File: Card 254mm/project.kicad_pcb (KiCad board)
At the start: 2 copper layers, 51.5 x 22 mm, 9 parts, among them J1 Conn_01x04, J2 Conn_01x10, J3 Conn_01x10, J4 Conn_01x10, J5 Conn_01x10, J6 Conn_01x10, U1 24LC32, X0 Card Edge

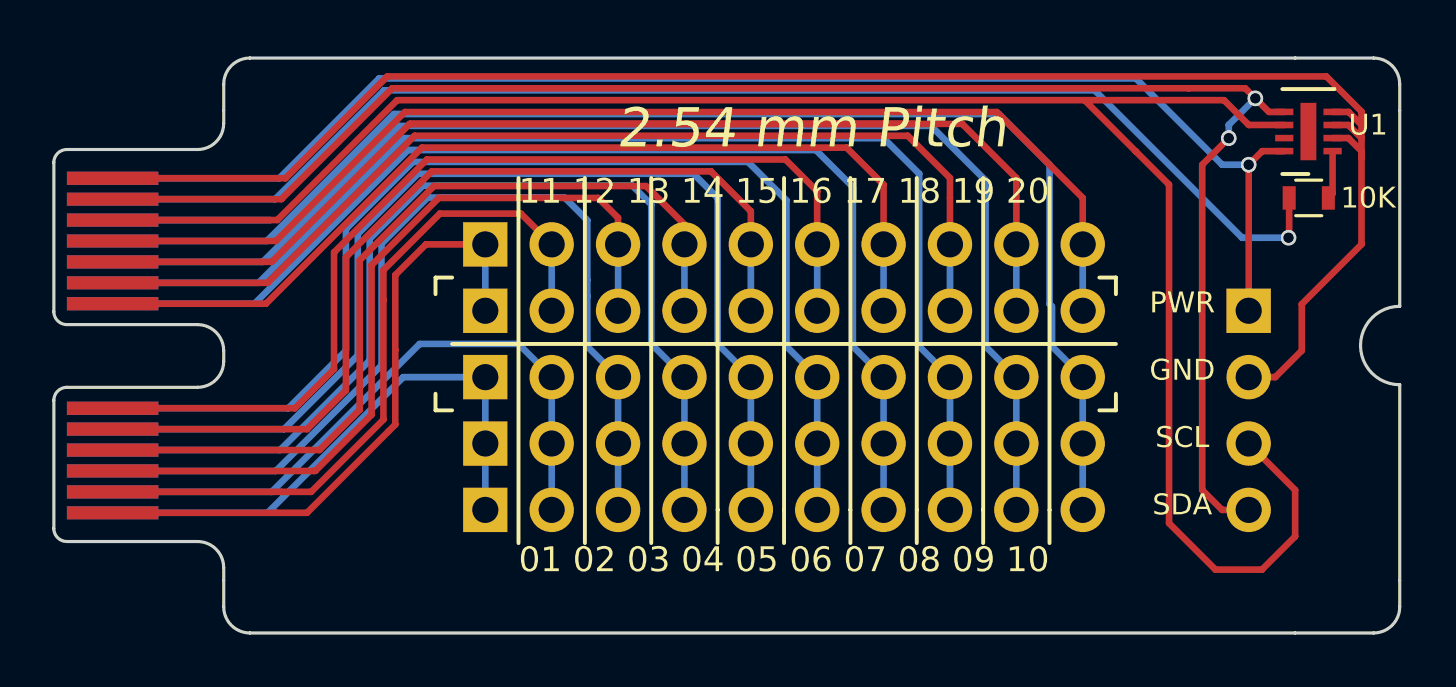
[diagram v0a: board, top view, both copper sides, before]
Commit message: EEPROM footprint update
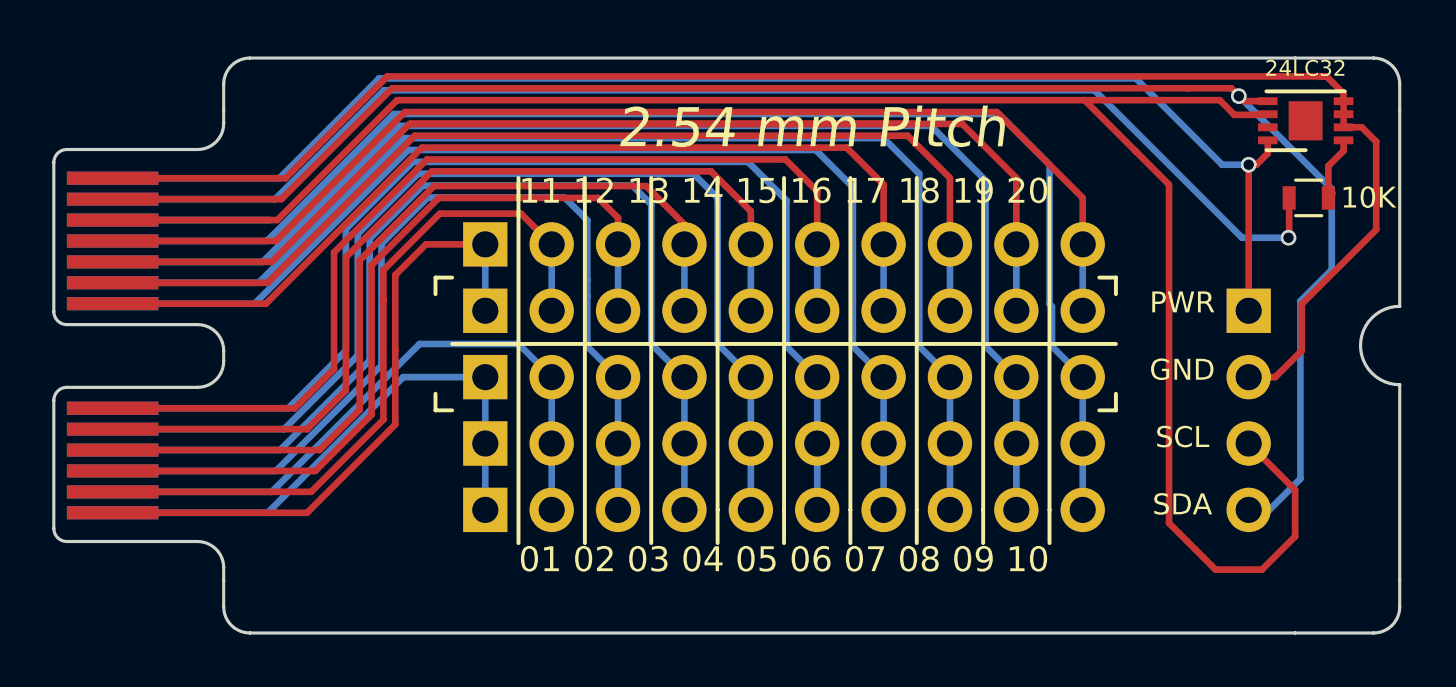
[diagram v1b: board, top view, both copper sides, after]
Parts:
- U1: footprint Package_DFN_QFN:DFN-8-1EP_2x3mm_P0.5mm_EP0.61x2.2mm -> footprints:DFN-8-1EP_3x2mm
- moved U1 0.43 mm to (47.9, -18.7)
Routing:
- net GND: track 66.7 -> 63.6 mm
- net Net-(R1-Pad1): track 1.86 -> 2.67 mm
- net /D3_SCL: track 75.0 -> 74.2 mm
- net /D2_SDA: track 64.9 -> 65.3 mm, vias 2 -> 1

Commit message: updates
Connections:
- J1 pad 1: +5V -> GND
- J1 pad 2: GND -> +5V
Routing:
- net +5V: track 53.4 -> 58.5 mm
- net GND: track 63.6 -> 61.7 mm
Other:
- board text added: "2.54mm Pitch"
- board text added: "GND PWR SCL SDA"
- board text removed: "2.54 mm Pitch"
- board text removed: "PWR GND SCL SDA"
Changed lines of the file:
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@@
     (thickness 1.6)
     (drawings 50)
-    (tracks 236)
+    (tracks 239)
     (zones 0)
     (modules 9)
@@
     )
     (pad 1 thru_hole rect (at 0 0) (size 1.7 1.7) (drill 1) (layers *.Cu *.Mask)
+      (net 22 GND))
+    (pad 2 thru_hole oval (at 0 2.54) (size 1.7 1.7) (drill 1) (layers *.Cu *.Mask)
       (net 24 +5V))
-    (pad 2 thru_hole oval (at 0 2.54) (size 1.7 1.7) (drill 1) (layers *.Cu *.Mask)
-      (net 22 GND))
     (pad 3 thru_hole oval (at 0 5.08) (size 1.7 1.7) (drill 1) (layers *.Cu *.Mask)
       (net 23 /D3_SCL))
@@
     )
   )
-  (gr_text "PWR\n\nGND\n\nSCL\n\nSDA" (at 43.18 -7.874) (layer B.SilkS)
+  (gr_text "GND\n\nPWR\n\nSCL\n\nSDA" (at 43.18 -7.874) (layer B.SilkS)
     (effects (font (size 0.8 0.8) (thickness 0.15)) (justify mirror))
   )
-  (gr_text "PWR\n\nGND\n\nSCL\n\nSDA" (at 43.18 -7.874) (layer F.SilkS)
+  (gr_text "GND\n\nPWR\n\nSCL\n\nSDA" (at 43.18 -7.874) (layer F.SilkS)
     (effects (font (size 0.8 0.8) (thickness 0.15)))
   )
@@
   )
   (gr_line (start 9.75 -19.5) (end 9.75 -0.5) (layer Dwgs.User) (width 0.1))
-  (gr_text "2.54 mm Pitch" (at 29 -18.415) (layer F.SilkS)
+  (gr_text "2.54mm Pitch" (at 29 -18.415) (layer F.SilkS)
     (effects (font (size 1.5 1.5) (thickness 0.25) italic))
   )
@@
   (segment (start 8.707934 -15.7) (end 12.950003 -19.94207) (width 0.254) (layer F.Cu) (net 21))
   (segment (start 2.25 -15.7) (end 8.707934 -15.7) (width 0.254) (layer F.Cu) (net 21) (status 10))
-  (segment (start 46.45 -19.45) (end 45.55 -19.45) (width 0.254) (layer F.Cu) (net 21))
+  (segment (start 46.45 -19.45) (end 45.55 -19.45) (width 0.254) (layer F.Cu) (net 21) (status 10))
   (segment (start 45.05793 -19.94207) (end 43.423864 -19.94207) (width 0.254) (layer F.Cu) (net 21))
   (via (at 45.343356 -19.643356) (size 0.6) (drill 0.4) (layers F.Cu B.Cu) (net 21))
@@
   (segment (start 48.9 -13) (end 47.7 -11.8) (width 0.254) (layer B.Cu) (net 21))
   (segment (start 47.7 -11.8) (end 47.7 -5) (width 0.254) (layer B.Cu) (net 21))
-  (segment (start 46.51 -3.81) (end 45.72 -3.81) (width 0.254) (layer B.Cu) (net 21))
-  (segment (start 47.7 -5) (end 46.51 -3.81) (width 0.254) (layer B.Cu) (net 21))
+  (segment (start 46.51 -3.81) (end 45.72 -3.81) (width 0.254) (layer B.Cu) (net 21) (status 30))
+  (segment (start 47.7 -5) (end 46.51 -3.81) (width 0.254) (layer B.Cu) (net 21) (status 20))
   (segment (start 8.865867 -16.5) (end 12.761946 -20.39608) (width 0.254) (layer F.Cu) (net 22))
   (segment (start 2.25 -16.5) (end 8.865867 -16.5) (width 0.254) (layer F.Cu) (net 22) (status 10))
-  (segment (start 49.35 -19.45) (end 49.35 -19.75) (width 0.254) (layer F.Cu) (net 22))
+  (segment (start 49.35 -19.45) (end 49.35 -19.75) (width 0.254) (layer F.Cu) (net 22) (status 10))
   (segment (start 48.70392 -20.39608) (end 48.49608 -20.39608) (width 0.254) (layer F.Cu) (net 22))
   (segment (start 49.35 -19.75) (end 48.70392 -20.39608) (width 0.254) (layer F.Cu) (net 22))
   (segment (start 48.49608 -20.39608) (end 48.69192 -20.39608) (width 0.254) (layer F.Cu) (net 22))
   (segment (start 12.761946 -20.39608) (end 48.49608 -20.39608) (width 0.254) (layer F.Cu) (net 22))
-  (segment (start 49.35 -19.45) (end 49.35 -18.95) (width 0.254) (layer F.Cu) (net 22))
-  (segment (start 49.35 -18.95) (end 49.35 -18.45) (width 0.254) (layer F.Cu) (net 22))
-  (segment (start 46.736 -8.89) (end 45.72 -8.89) (width 0.254) (layer F.Cu) (net 22))
-  (segment (start 47.752 -9.906) (end 46.736 -8.89) (width 0.254) (layer F.Cu) (net 22))
-  (segment (start 50.6 -14.532) (end 47.752 -11.684) (width 0.254) (layer F.Cu) (net 22))
-  (segment (start 47.752 -11.684) (end 47.752 -9.906) (width 0.254) (layer F.Cu) (net 22))
+  (segment (start 49.35 -19.45) (end 49.35 -18.95) (width 0.254) (layer F.Cu) (net 22) (status 30))
+  (segment (start 49.35 -18.95) (end 49.35 -18.45) (width 0.254) (layer F.Cu) (net 22) (status 30))
   (segment (start 50.6 -17.9) (end 50.6 -14.532) (width 0.254) (layer F.Cu) (net 22))
   (segment (start 50.05 -18.45) (end 50.6 -17.9) (width 0.254) (layer F.Cu) (net 22))
-  (segment (start 49.35 -18.45) (end 50.05 -18.45) (width 0.254) (layer F.Cu) (net 22))
+  (segment (start 49.35 -18.45) (end 50.05 -18.45) (width 0.254) (layer F.Cu) (net 22) (status 10))
+  (segment (start 47.498 -11.43) (end 47.884 -11.816) (width 0.254) (layer F.Cu) (net 22))
+  (segment (start 45.72 -11.43) (end 47.498 -11.43) (width 0.254) (layer F.Cu) (net 22))
+  (segment (start 47.884 -11.816) (end 47.752 -11.684) (width 0.254) (layer F.Cu) (net 22))
+  (segment (start 50.6 -14.532) (end 47.884 -11.816) (width 0.254) (layer F.Cu) (net 22))
   (segment (start 13.13806 -19.48806) (end 39.43994 -19.48806) (width 0.254) (layer F.Cu) (net 23))
   (segment (start 8.55 -14.9) (end 13.13806 -19.48806) (width 0.254) (layer F.Cu) (net 23))
@@
   (segment (start 45.72 -6.35) (end 47.498 -4.572) (width 0.254) (layer F.Cu) (net 23) (status 10))
   (segment (start 45.172999 -18.927001) (end 44.61194 -19.48806) (width 0.254) (layer F.Cu) (net 23))
-  (segment (start 46.327001 -18.927001) (end 45.172999 -18.927001) (width 0.254) (layer F.Cu) (net 23))
-  (segment (start 46.35 -18.95) (end 46.327001 -18.927001) (width 0.254) (layer F.Cu) (net 23))
-  (segment (start 46.45 -18.95) (end 46.35 -18.95) (width 0.254) (layer F.Cu) (net 23))
+  (segment (start 46.327001 -18.927001) (end 45.172999 -18.927001) (width 0.254) (layer F.Cu) (net 23) (status 10))
+  (segment (start 46.35 -18.95) (end 46.327001 -18.927001) (width 0.254) (layer F.Cu) (net 23) (status 30))
+  (segment (start 46.45 -18.95) (end 46.35 -18.95) (width 0.254) (layer F.Cu) (net 23) (status 30))
   (segment (start 44.61194 -19.48806) (end 39.43994 -19.48806) (width 0.254) (layer F.Cu) (net 23))
   (via (at 45.72 -17.018) (size 0.6) (drill 0.4) (layers F.Cu B.Cu) (net 24))
-  (segment (start 45.72 -11.43) (end 45.72 -17.018) (width 0.254) (layer F.Cu) (net 24) (status 10))
   (segment (start 8.626 -16.5) (end 2.25 -16.5) (width 0.254) (layer B.Cu) (net 24) (status 20))
   (segment (start 12.446 -20.32) (end 8.626 -16.5) (width 0.254) (layer B.Cu) (net 24))
@@
   (segment (start 44.704 -17.018) (end 41.402 -20.32) (width 0.254) (layer B.Cu) (net 24))
   (segment (start 45.72 -17.018) (end 44.704 -17.018) (width 0.254) (layer B.Cu) (net 24))
-  (segment (start 46.45 -17.95) (end 46.45 -17.45) (width 0.254) (layer F.Cu) (net 24))
+  (segment (start 46.45 -17.95) (end 46.45 -17.45) (width 0.254) (layer F.Cu) (net 24) (status 10))
   (segment (start 46.018 -17.018) (end 45.72 -17.018) (width 0.254) (layer F.Cu) (net 24))
   (segment (start 46.45 -17.45) (end 46.018 -17.018) (width 0.254) (layer F.Cu) (net 24))
+  (segment (start 45.72 -8.89) (end 44.21 -8.89) (width 0.254) (layer F.Cu) (net 24))
+  (segment (start 44.21 -8.89) (end 43.7 -9.4) (width 0.254) (layer F.Cu) (net 24))
+  (segment (start 43.7 -14.998) (end 45.72 -17.018) (width 0.254) (layer F.Cu) (net 24))
+  (segment (start 43.7 -9.4) (end 43.7 -14.998) (width 0.254) (layer F.Cu) (net 24))
   (segment (start 48.931 -15.911) (end 48.768 -15.748) (width 0.254) (layer F.Cu) (net 25) (status 30))
-  (segment (start 49.35 -17.95) (end 49.35 -17.55) (width 0.254) (layer F.Cu) (net 25))
-  (segment (start 48.768 -16.968) (end 48.768 -15.748) (width 0.254) (layer F.Cu) (net 25))
+  (segment (start 49.35 -17.95) (end 49.35 -17.55) (width 0.254) (layer F.Cu) (net 25) (status 10))
+  (segment (start 48.768 -16.968) (end 48.768 -15.748) (width 0.254) (layer F.Cu) (net 25) (status 20))
   (segment (start 49.35 -17.55) (end 48.768 -16.968) (width 0.254) (layer F.Cu) (net 25))
   (via (at 47.244 -14.224) (size 0.6) (drill 0.4) (layers F.Cu B.Cu) (net 26))

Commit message: Updates
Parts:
- moved U1 2.91 mm to (45.0, -18.5)
- moved R1 2.75 mm to (48.0, -18.5), turned to 90 degrees
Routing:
- net /D3_SCL: track 74.2 -> 59.6 mm
- net /D2_SDA: track 65.3 -> 62.3 mm
- net /A: track 50.6 -> 52.8 mm
- net +5V: track 58.5 -> 56.3 mm
- net Net-(R1-Pad1): track 2.67 -> 1.55 mm
- net GND: track 61.7 -> 62.6 mm
